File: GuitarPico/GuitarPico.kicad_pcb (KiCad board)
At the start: 2 copper layers, 100 x 100 mm, 112 parts, among them J1 INPUT, J2 INPUT, J3 OUTPUT, J4 OUTPUT, J5 Barrel_Jack_Switch, J6 INPUT, J7 INPUT, J8 INPUT, J9 INPUT, Q1 2N3904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

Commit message: Before replacing with buttons
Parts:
- added C30: 100 pF, Capacitor_THT:C_Disc_D5.0mm_W2.5mm_P5.00mm, F.Cu at (103.8, 146.5)
- C12: value 330 nF -> 220 pF
- C13: value 2200 pF -> 220 pF
- R13, R14, R15: value 1k -> 10k
- moved C27 1.60 mm to (45.2, 147.1)
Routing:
- net VREF: track 271.0 -> 264.8 mm
- net Net-(J8-PadT1): track 81.5 -> 75.4 mm
- net Net-(J9-PadT1): track 110.6 -> 105.6 mm
- net CTRLIN: track 51.5 -> 54.8 mm
- net Net-(C27-Pad2): track 67.0 -> 65.6 mm
- net Net-(J7-PadT1): track 41.4 -> 40.4 mm

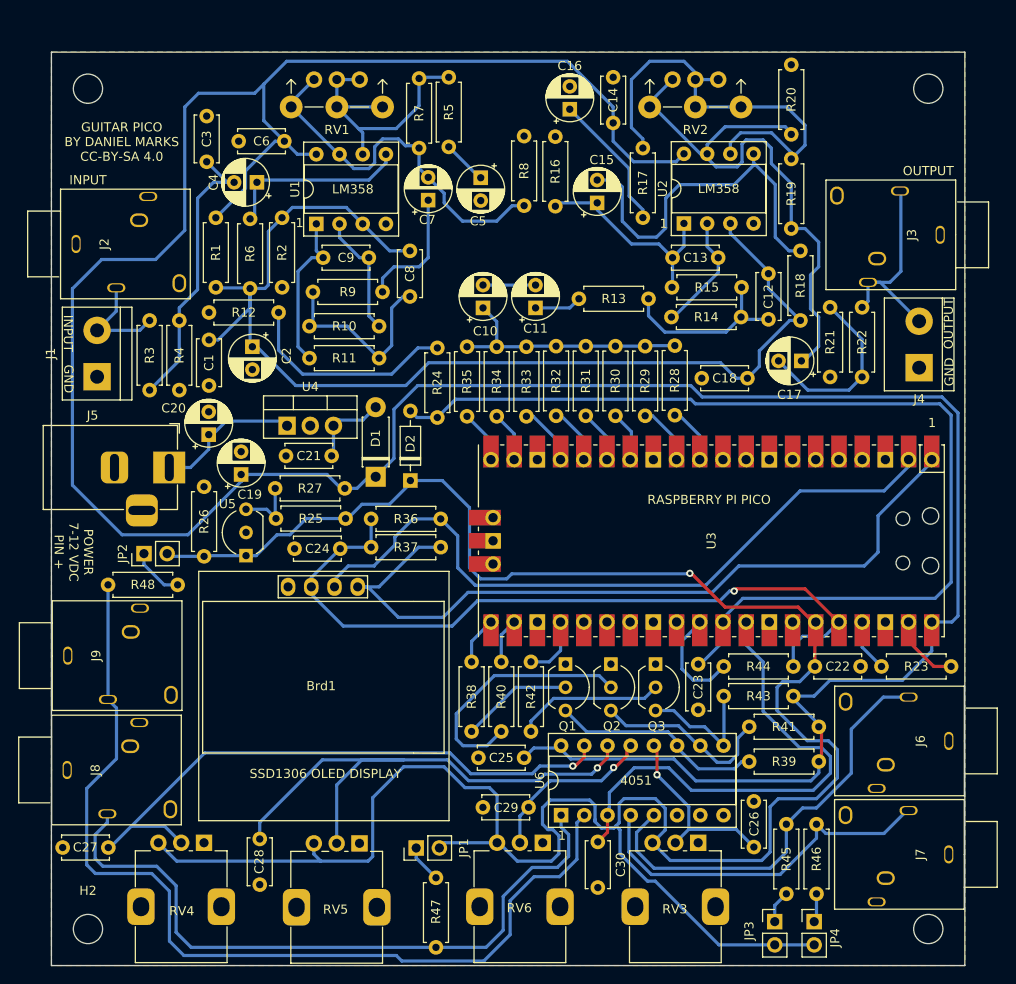
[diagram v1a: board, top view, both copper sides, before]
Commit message: replaced with buttons
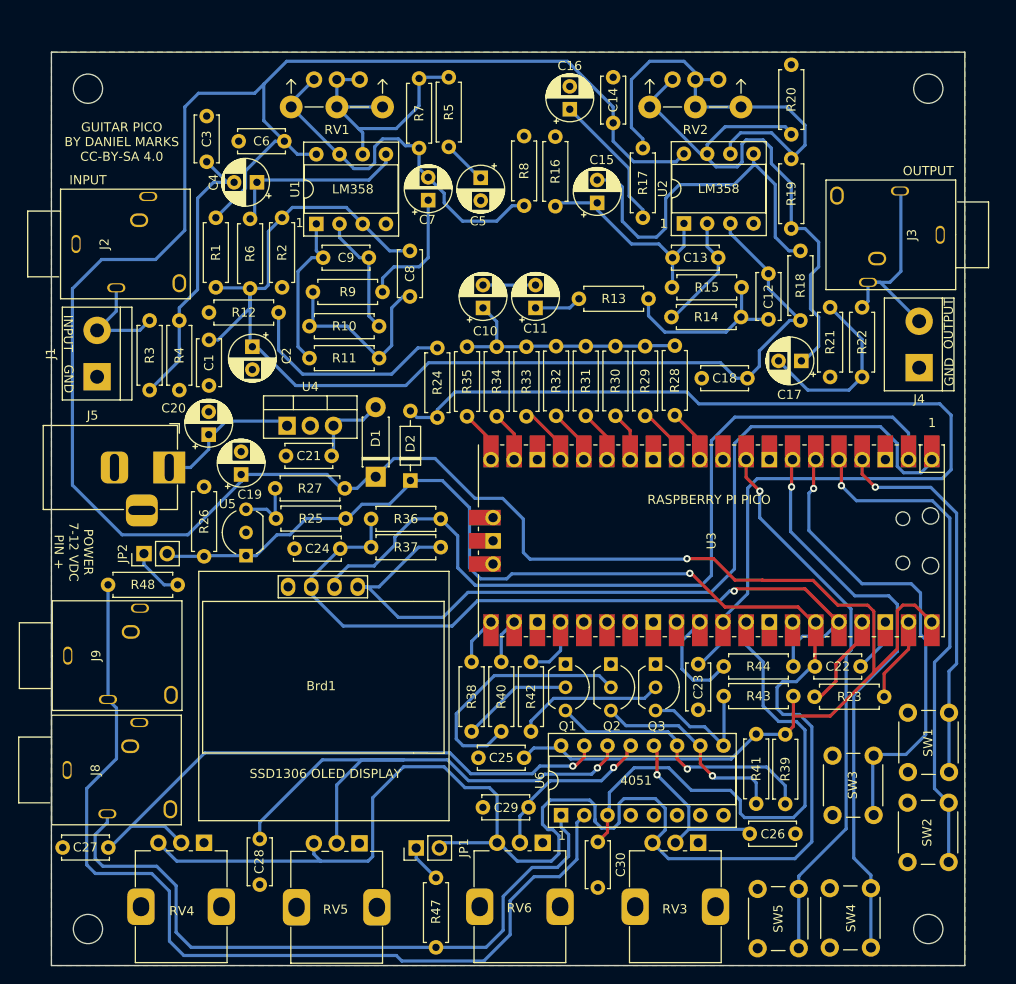
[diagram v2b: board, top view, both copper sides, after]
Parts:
- removed J6, J7: INPUT, GuitarPico:PJ-3240-35mm-stereo
- removed JP3, JP4: POWER, Connector_PinHeader_2.54mm:PinHeader_1x02_P2.54mm_Vertical
- removed R45, R46: 10k, Resistor_THT:R_Axial_DIN0207_L6.3mm_D2.5mm_P7.62mm_Horizontal
- added SW1: SW_Push, Button_Switch_THT:SW_PUSH_6mm, F.Cu at (137.8, 138.8)
- added SW2: SW_Push, Button_Switch_THT:SW_PUSH_6mm, F.Cu at (137.7, 148.7)
- added SW3: SW_Push, Button_Switch_THT:SW_PUSH_6mm, F.Cu at (129.5, 143.5)
- added SW4: SW_Push, Button_Switch_THT:SW_PUSH_6mm, F.Cu at (129.2, 158.0)
- added SW5: SW_Push, Button_Switch_THT:SW_PUSH_6mm, F.Cu at (121.3, 158.1)
- moved R23 8.04 mm to (127.5, 130.6)
- moved R41 6.90 mm to (121.2, 134.7), turned to -90 degrees
- moved C26 5.76 mm to (125.5, 145.6), turned to 180 degrees
- moved R39 4.73 mm to (124.3, 134.7), turned to -90 degrees
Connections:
- U3 pad 4: unconnected-(U3-Pad4) -> Net-(U3-Pad4)
- U3 pad 5: unconnected-(U3-Pad5) -> Net-(U3-Pad5)
- U3 pad 6: unconnected-(U3-Pad6) -> Net-(U3-Pad6)
- U3 pad 7: unconnected-(U3-Pad7) -> Net-(U3-Pad7)
- U3 pad 9: unconnected-(U3-Pad9) -> Net-(U3-Pad9)
- U6 pad 4: Net-(J7-PadT1) -> unconnected-(U6-Pad4)
- U6 pad 5: Net-(J6-PadT1) -> unconnected-(U6-Pad5)
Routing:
- net Net-(U3-Pad7): track 0.00 -> 63.3 mm, vias 0 -> 1
- net Net-(U3-Pad9): track 0.00 -> 60.6 mm, vias 0 -> 1
- net Net-(U3-Pad5): track 0.00 -> 55.3 mm, vias 0 -> 1
- net Net-(U3-Pad6): track 0.00 -> 53.4 mm, vias 0 -> 1
- net Net-(J6-PadT1): track 47.6 -> 0.00 mm
- net Net-(U3-Pad4): track 0.00 -> 42.4 mm, vias 0 -> 1
- net Net-(J7-PadT1): track 40.4 -> 0.00 mm
- net +5V: track 340.1 -> 307.5 mm, vias 0 -> 1
- net VREF: track 264.8 -> 233.0 mm
- net SCL: track 78.1 -> 91.9 mm
- net SDA: track 84.8 -> 96.1 mm
- net Net-(Q1-Pad3): track 23.5 -> 30.8 mm, vias 0 -> 1
- net GND: track 0.00 -> 5.99 mm
- net Net-(R23-Pad1): track 5.74 -> 10.7 mm
- net Net-(JP3-Pad1): track 3.57 -> 0.00 mm
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
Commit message: Fixed TL431 wiring problem
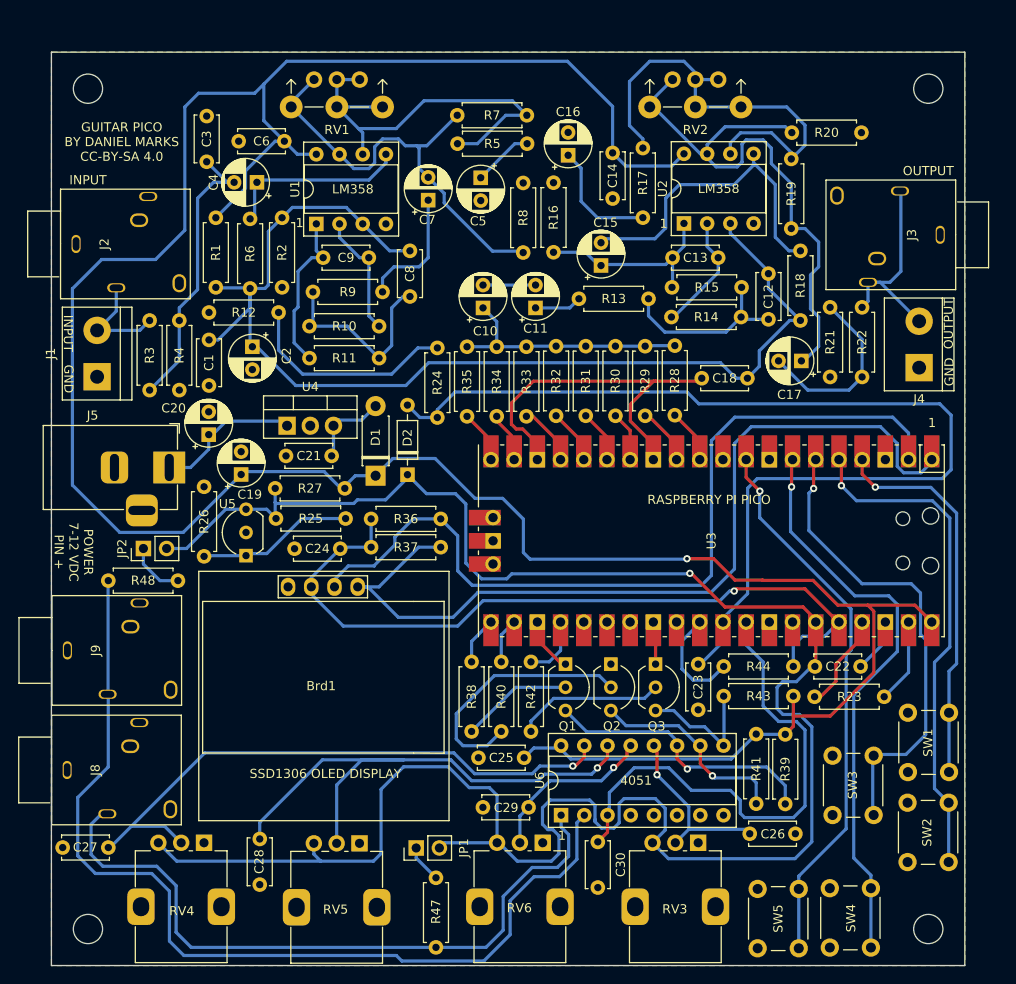
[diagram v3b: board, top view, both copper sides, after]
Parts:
- moved R20 10.7 mm to (132.7, 68.8), turned to 180 degrees
- moved R5 7.33 mm to (88.5, 70.0), turned to 0 degrees
- moved C15 6.87 mm to (104.2, 83.4)
- moved R7 5.51 mm to (88.4, 66.9), turned to 0 degrees
- moved R8 5.13 mm to (95.7, 74.3)
- moved R16 5.04 mm to (99.0, 74.3)
- moved C16 5.04 mm to (100.6, 71.3)
- moved C14 3.28 mm to (105.4, 71.0), turned to -90 degrees
- moved D2 0.72 mm to (83.0, 106.3)
- moved J9 0.57 mm to (44.0, 125.5)
- moved JP2 0.56 mm to (54.1, 114.3)
- moved R48 0.46 mm to (57.9, 117.9)
- moved D1 0.12 mm to (79.5, 106.4)
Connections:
- R25 pad 1: VREF -> Net-(R25-Pad1)
- R25 pad 2: Net-(R25-Pad2) -> VREF
- R26 pad 2: VREF -> Net-(R25-Pad1)
- R27 pad 1: Net-(R25-Pad2) -> VREF
- U5 pad 1: VREF -> Net-(R25-Pad1)
- U5 pad 3: Net-(R25-Pad2) -> VREF
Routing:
- net GND: track 5.99 -> 57.5 mm
- net Net-(R25-Pad1): track 0.00 -> 16.8 mm
- net Net-(R5-Pad1): track 30.8 -> 46.1 mm
- net Net-(C7-Pad2): track 41.0 -> 48.1 mm
- net Net-(R25-Pad2): track 7.04 -> 0.00 mm
- net Net-(C15-Pad2): track 40.8 -> 35.9 mm
- net +5V: track 307.5 -> 303.3 mm
- net VREF: track 233.0 -> 237.0 mm
- net Net-(C16-Pad1): track 15.2 -> 13.1 mm
- net Net-(C13-Pad1): track 23.5 -> 21.5 mm
- net Net-(C5-Pad1): track 4.90 -> 6.63 mm
- net Net-(J8-PadT1): track 75.4 -> 76.2 mm
- net TOADC: track 112.9 -> 113.5 mm
- net Net-(J9-PadT1): track 105.6 -> 106.2 mm

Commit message: Added VGA connector!
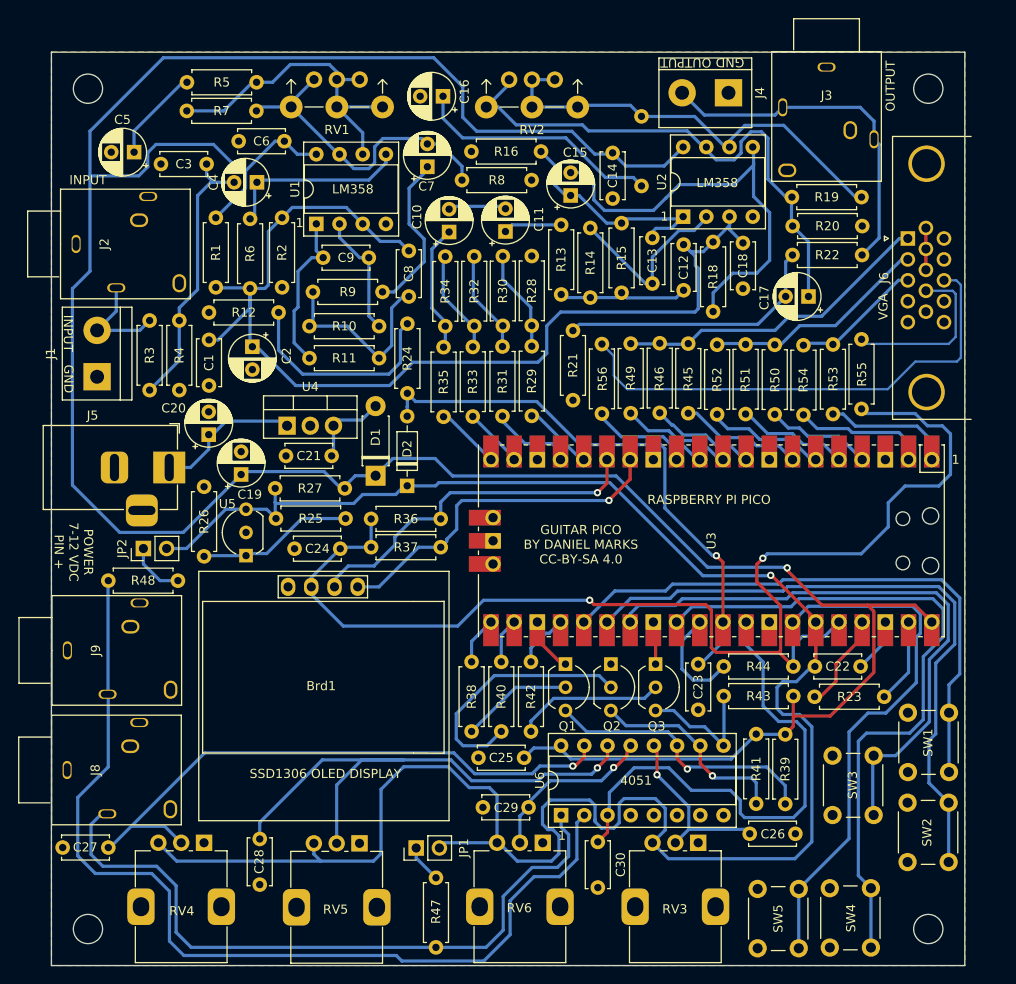
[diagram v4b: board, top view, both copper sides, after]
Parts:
- added J6: VGA, Connector_Dsub:DSUB-15-HD_Female_Horizontal_P2.29x1.98mm_EdgePinOffset3.03mm_Housed_MountingHolesOffset4.94mm, F.Cu at (137.8, 80.4)
- added R45: 2k2, Resistor_THT:R_Axial_DIN0207_L6.3mm_D2.5mm_P7.62mm_Horizontal, F.Cu at (113.7, 91.9)
- added R46: 1k, Resistor_THT:R_Axial_DIN0207_L6.3mm_D2.5mm_P7.62mm_Horizontal, F.Cu at (110.6, 91.9)
- added R49: 470R, Resistor_THT:R_Axial_DIN0207_L6.3mm_D2.5mm_P7.62mm_Horizontal, F.Cu at (107.4, 91.9)
- added R50: 2k2, Resistor_THT:R_Axial_DIN0207_L6.3mm_D2.5mm_P7.62mm_Horizontal, F.Cu at (123.2, 92.0)
- added R51: 1k, Resistor_THT:R_Axial_DIN0207_L6.3mm_D2.5mm_P7.62mm_Horizontal, F.Cu at (120.0, 92.0)
- added R52: 470R, Resistor_THT:R_Axial_DIN0207_L6.3mm_D2.5mm_P7.62mm_Horizontal, F.Cu at (116.9, 92.0)
- added R53: 1k, Resistor_THT:R_Axial_DIN0207_L6.3mm_D2.5mm_P7.62mm_Horizontal, F.Cu at (129.6, 92.0)
- added R54: 390R, Resistor_THT:R_Axial_DIN0207_L6.3mm_D2.5mm_P7.62mm_Horizontal, F.Cu at (126.3, 92.1)
- added R55: 150R, Resistor_THT:R_Axial_DIN0207_L6.3mm_D2.5mm_P7.62mm_Horizontal, F.Cu at (132.7, 99.1)
- added R56: 100R, Resistor_THT:R_Axial_DIN0207_L6.3mm_D2.5mm_P7.62mm_Horizontal, F.Cu at (104.3, 92.0)
- R17: moved to B.Cu
- R28, R29, R31, R33, R35: value TBD -> 2k
- R30, R32, R34: value TBD -> 1k
- moved C5 38.1 mm to (53.0, 71.0), turned to 180 degrees
- moved J4 36.6 mm to (118.1, 64.5), turned to 180 degrees
- moved R21 28.3 mm to (101.1, 98.1)
- moved J3 24.5 mm to (128.9, 59.9), turned to 0 degrees
- moved R5 23.0 mm to (66.5, 63.3), turned to 180 degrees
- moved R7 22.0 mm to (66.4, 66.4), turned to 180 degrees
- moved RV2 17.9 mm to (96.6, 63.0)
- moved R14 16.6 mm to (103.0, 86.9), turned to 90 degrees
- moved R28 15.8 mm to (96.6, 89.9), turned to 90 degrees
- moved C16 15.1 mm to (86.9, 64.8), turned to 180 degrees
- moved C18 14.8 mm to (119.7, 80.9), turned to -90 degrees
- moved R15 13.2 mm to (106.4, 86.3), turned to 90 degrees
- moved R30 12.5 mm to (93.4, 90.0), turned to 90 degrees
- moved R29 12.4 mm to (96.6, 92.2)
- moved R18 11.6 mm to (116.4, 88.4), turned to 90 degrees
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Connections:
- R28 pad 1: FROMDAC -> Net-(R28-Pad1)
- R28 pad 2: Net-(R28-Pad2) -> GND
- R29 pad 1: FROMDAC -> Net-(R28-Pad1)
- R30 pad 1: FROMDAC -> Net-(R30-Pad1)
- R30 pad 2: Net-(R30-Pad2) -> Net-(R28-Pad1)
- R31 pad 1: FROMDAC -> Net-(R30-Pad1)
- R32 pad 1: FROMDAC -> Net-(R32-Pad1)
- R32 pad 2: Net-(R32-Pad2) -> Net-(R30-Pad1)
- R33 pad 1: FROMDAC -> Net-(R32-Pad1)
- R34 pad 2: Net-(R34-Pad2) -> Net-(R32-Pad1)
- SW1 pad 2: Net-(SW1-Pad2) -> BUTTON1
- SW2 pad 2: Net-(SW2-Pad2) -> BUTTON2
- SW3 pad 2: Net-(SW3-Pad2) -> BUTTON3
- SW4 pad 2: Net-(SW4-Pad2) -> BUTTON4
- SW5 pad 2: Net-(SW5-Pad2) -> BUTTON5
- U3 pad 1: SDA -> B0
- U3 pad 10: unconnected-(U3-Pad10) -> R2
- U3 pad 11: Net-(R28-Pad2) -> SYNC
- U3 pad 12: Net-(R29-Pad2) -> unconnected-(U3-Pad12)
- U3 pad 14: Net-(R30-Pad2) -> SDA
- U3 pad 15: Net-(R31-Pad2) -> SCL
- U3 pad 16: Net-(R32-Pad2) -> Net-(R29-Pad2)
- U3 pad 17: Net-(R33-Pad2) -> Net-(R31-Pad2)
- U3 pad 19: Net-(R34-Pad2) -> Net-(R33-Pad2)
- U3 pad 2: SCL -> B1
- U3 pad 25: unconnected-(U3-Pad25) -> BUTTON1
- U3 pad 26: unconnected-(U3-Pad26) -> BUTTON2
- U3 pad 27: unconnected-(U3-Pad27) -> BUTTON3
- U3 pad 29: unconnected-(U3-Pad29) -> BUTTON4
- U3 pad 34: unconnected-(U3-Pad34) -> BUTTON5
- U3 pad 4: Net-(SW1-Pad2) -> G0
- U3 pad 5: Net-(SW2-Pad2) -> G1
- U3 pad 6: Net-(SW3-Pad2) -> G2
- U3 pad 7: Net-(SW4-Pad2) -> R0
- U3 pad 9: Net-(SW5-Pad2) -> R1
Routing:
- net BUTTON4: track 0.00 -> 75.0 mm
- net BUTTON2: track 0.00 -> 70.9 mm
- net BUTTON3: track 0.00 -> 66.2 mm
- net BUTTON1: track 0.00 -> 63.5 mm
- net Net-(SW4-Pad2): track 63.3 -> 0.00 mm, vias 1 -> 0
- net Net-(SW5-Pad2): track 60.6 -> 0.00 mm, vias 1 -> 0
- net BUTTON5: track 0.00 -> 58.3 mm
- net SDA: track 96.1 -> 38.5 mm, vias 0 -> 1
- net Net-(SW2-Pad2): track 55.3 -> 0.00 mm, vias 1 -> 0
- net Net-(J6-Pad13): track 0.00 -> 54.1 mm
- net Net-(SW3-Pad2): track 53.4 -> 0.00 mm, vias 1 -> 0
- net SCL: track 92.1 -> 39.2 mm, vias 0 -> 1
- net TOADC: track 113.5 -> 61.0 mm, vias 0 -> 1
- net +3V3: track 83.6 -> 134.9 mm, vias 1 -> 2
- net Net-(SW1-Pad2): track 42.4 -> 0.00 mm, vias 1 -> 0
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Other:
- board text added: "VGA"

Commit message: Flipped resistor
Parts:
- R17: moved to F.Cu
- moved RV2 1.61 mm to (98.2, 63.0)
- moved R21 1.02 mm to (100.1, 98.1)
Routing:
- net Net-(R17-Pad1): track 48.2 -> 46.6 mm
- net Net-(C17-Pad1): track 59.3 -> 57.9 mm
- net Net-(C17-Pad2): track 29.7 -> 30.7 mm

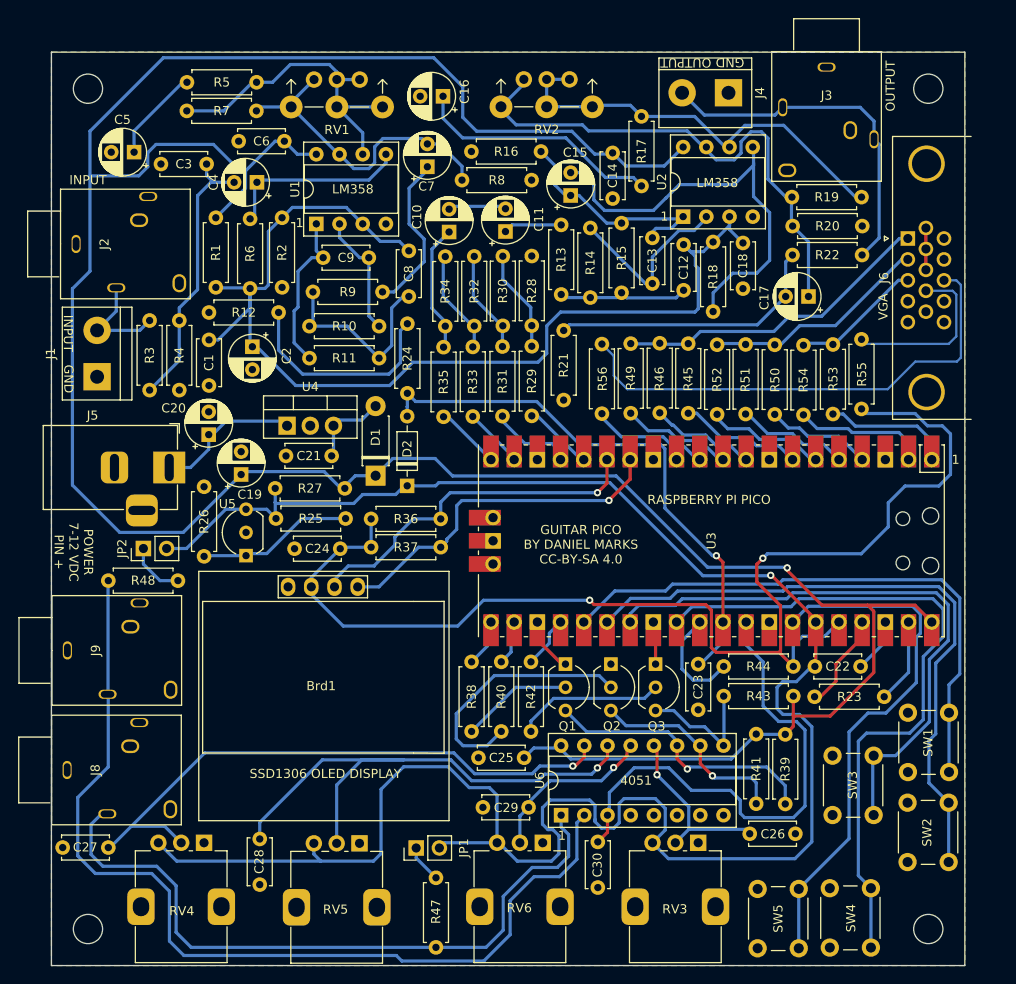
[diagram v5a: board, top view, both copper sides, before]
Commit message: Added CAD pedal
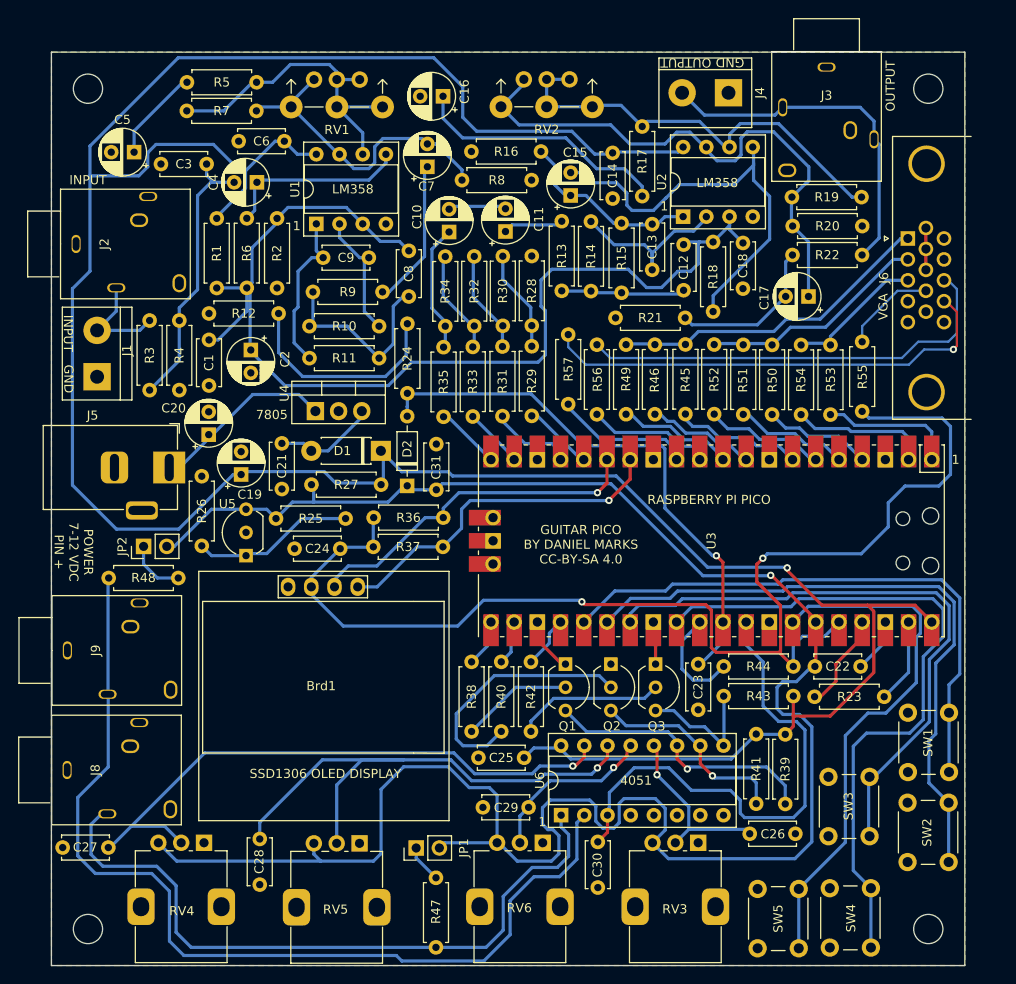
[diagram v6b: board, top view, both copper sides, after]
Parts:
- added C31: 10 nF, Capacitor_THT:C_Disc_D5.0mm_W2.5mm_P5.00mm, F.Cu at (86.1, 102.9)
- added R57: 100R, Resistor_THT:R_Axial_DIN0207_L6.3mm_D2.5mm_P7.62mm_Horizontal, F.Cu at (100.6, 90.9)
- moved R21 10.6 mm to (105.8, 89.1), turned to 0 degrees
- moved C21 5.62 mm to (69.2, 102.8), turned to -90 degrees
- moved R27 3.99 mm to (72.5, 107.3)
- moved U4 3.49 mm to (72.9, 99.3)
- moved D1 2.78 mm to (80.1, 103.7), turned to 180 degrees
- moved SW3 2.36 mm to (129.1, 145.8)
- moved C13 1.50 mm to (109.8, 78.8)
- moved R26 1.18 mm to (60.5, 106.4)
- moved R17 1.11 mm to (108.7, 68.1)
- moved R14 0.71 mm to (103.1, 86.2)
- moved R56 0.55 mm to (103.7, 92.0)
- moved R2 0.55 mm to (68.7, 85.8)
- moved R46 0.55 mm to (110.1, 92.0)
- moved R49 0.52 mm to (106.9, 92.0)
- moved R13 0.40 mm to (99.9, 78.5)
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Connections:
- J6 pad 14: unconnected-(J6-Pad14) -> Net-(J6-Pad14)
- U3 pad 12: unconnected-(U3-Pad12) -> VSYNC
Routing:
- net Net-(J6-Pad14): track 0.00 -> 51.2 mm, vias 0 -> 1
- net VSYNC: track 0.00 -> 15.1 mm
- net Net-(C17-Pad2): track 30.7 -> 17.5 mm
- net Net-(J6-Pad9): track 19.0 -> 10.3 mm
- net Net-(J6-Pad13): track 54.1 -> 47.8 mm
- net Net-(C20-Pad1): track 15.9 -> 20.1 mm
- net Net-(C17-Pad1): track 57.9 -> 61.2 mm
- net Net-(C13-Pad1): track 25.1 -> 21.8 mm
- net Net-(C21-Pad1): track 8.88 -> 11.3 mm
- net Net-(C15-Pad2): track 47.9 -> 46.2 mm
- net Net-(C7-Pad1): track 17.8 -> 16.2 mm
- net BUTTON3: track 66.2 -> 67.7 mm
- net Net-(C16-Pad1): track 27.2 -> 28.4 mm
- net Net-(R17-Pad1): track 46.6 -> 47.6 mm
- net SCL: track 39.2 -> 38.2 mm
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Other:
- board text added: "7805"
